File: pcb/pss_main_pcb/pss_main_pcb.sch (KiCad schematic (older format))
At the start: 0 parts

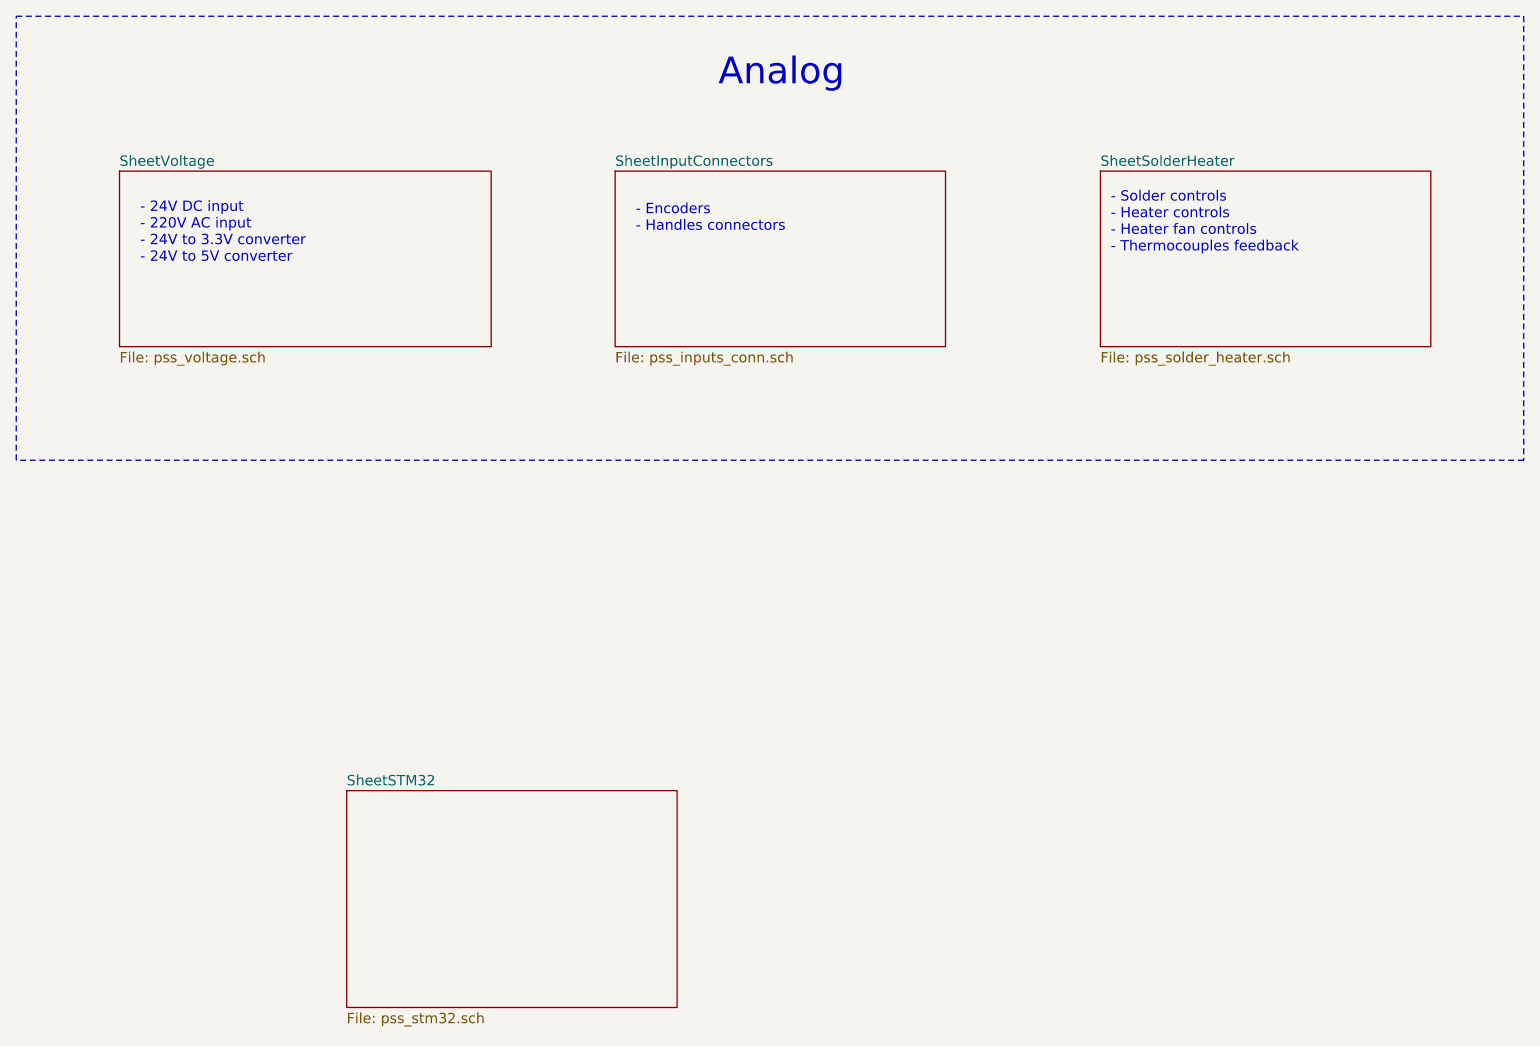
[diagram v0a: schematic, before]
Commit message: Add stm32 schematics
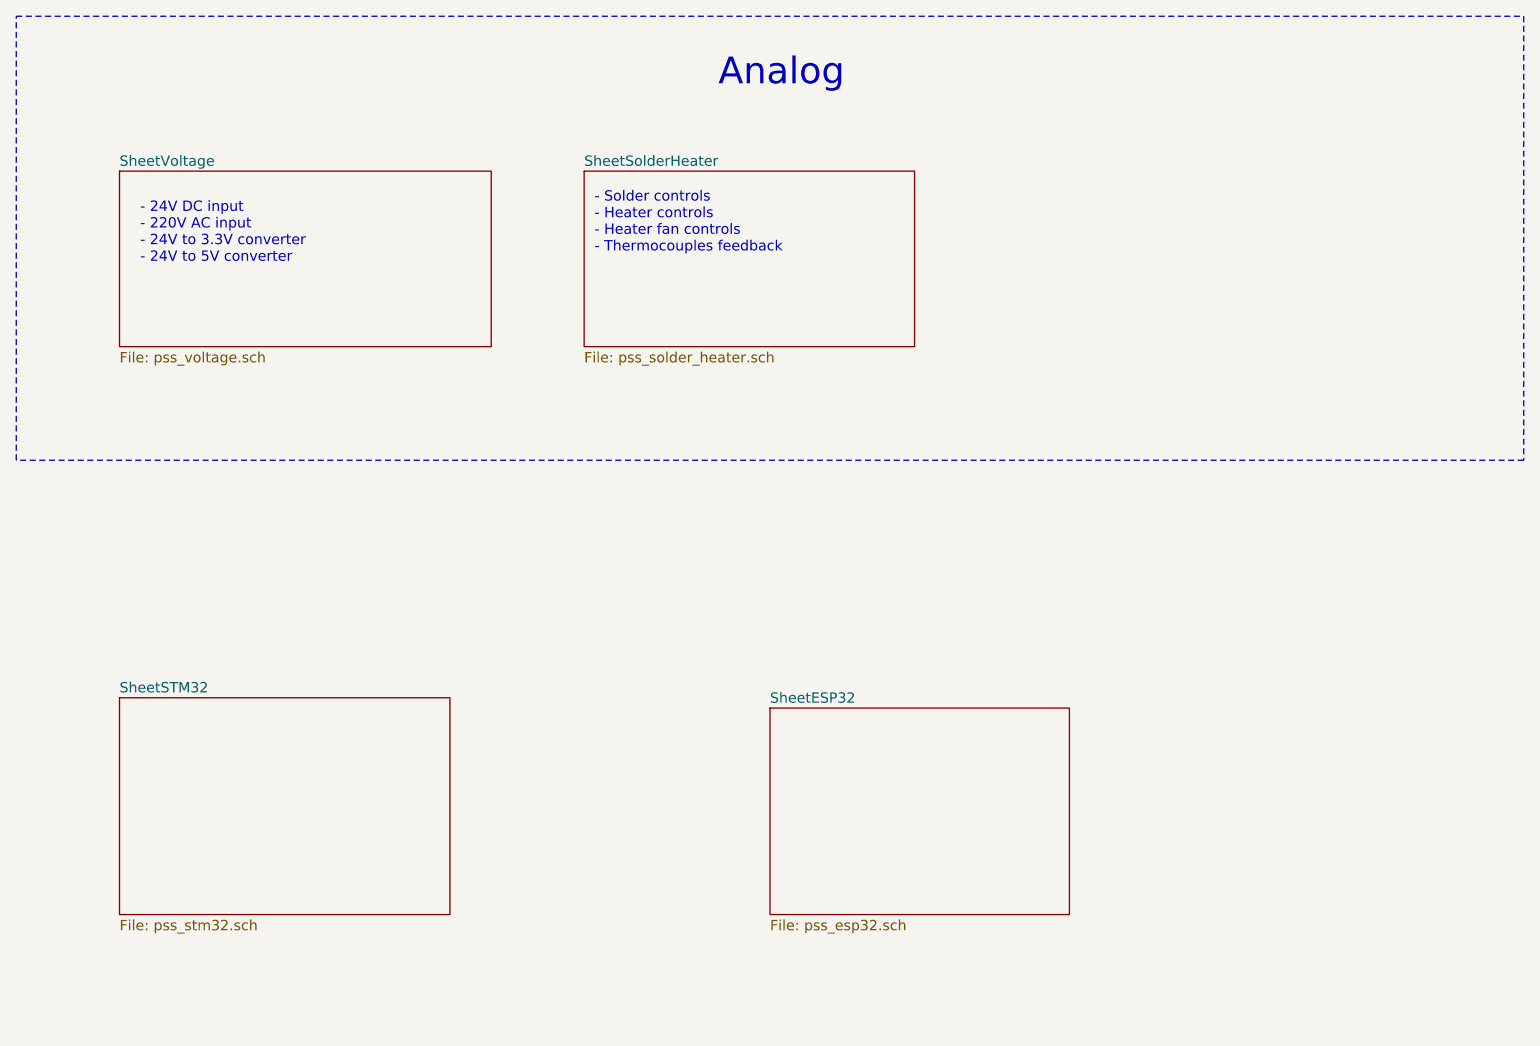
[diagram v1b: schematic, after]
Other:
- note removed: "- Encoders\n- Handles connectors"
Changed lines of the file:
@@
 EESchema Schematic File Version 4
-LIBS:pss_main_pcb-cache
-EELAYER 26 0
+EELAYER 30 0
 EELAYER END
 $Descr A4 11693 8268
@@
 $EndSheet
 $Sheet
-S 5450 1850 1600 850
-U 5EE027BC
-F0 "SheetInputConnectors" 50
-F1 "pss_inputs_conn.sch" 50
-$EndSheet
-$Sheet
-S 7800 1850 1600 850
+S 5300 1850 1600 850
 U 5EE1CBE0
 F0 "SheetSolderHeater" 50
@@
 Text Notes 3150 2300 0    50   ~ 0
 - 24V DC input\n- 220V AC input \n- 24V to 3.3V converter\n- 24V to 5V converter
-Text Notes 5550 2150 0    50   ~ 0
-- Encoders\n- Handles connectors
-Text Notes 7850 2250 0    50   ~ 0
+Text Notes 5350 2250 0    50   ~ 0
 - Solder controls\n- Heater controls\n- Heater fan controls\n- Thermocouples feedback\n
 Wire Notes Line
@@
 Analog
 $Sheet
-S 4150 4850 1600 1050
+S 3050 4400 1600 1050
 U 5EE5A305
 F0 "SheetSTM32" 50
 F1 "pss_stm32.sch" 50
 $EndSheet
+$Sheet
+S 6200 4450 1450 1000
+U 5ED3D5DF
+F0 "SheetESP32" 50
+F1 "pss_esp32.sch" 50
+$EndSheet
 $EndSCHEMATC

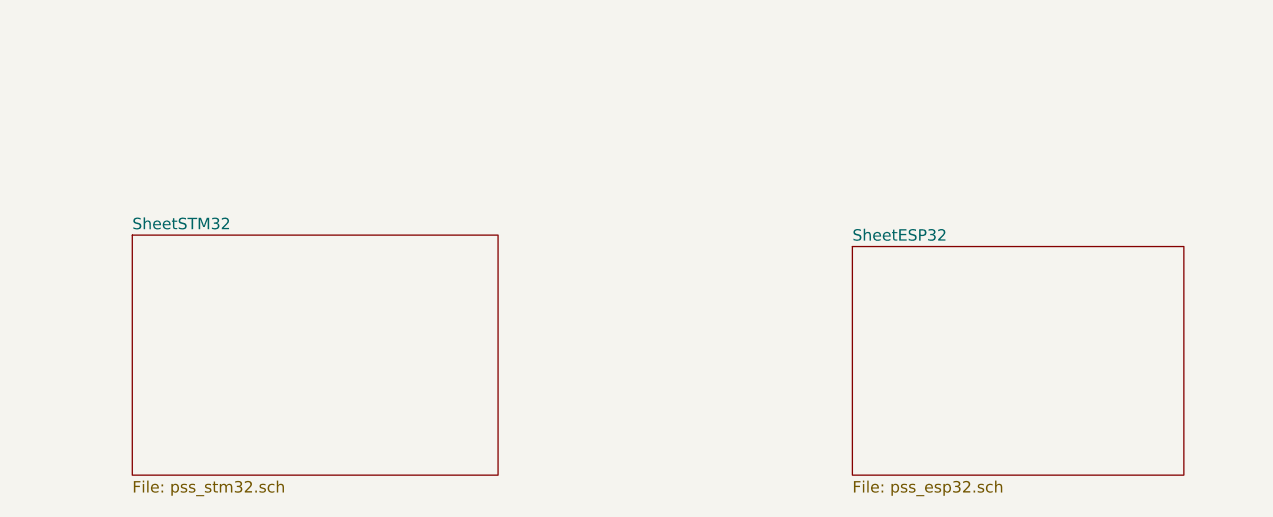
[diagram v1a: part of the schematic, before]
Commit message: Add ESP32 to display and STM32 connections
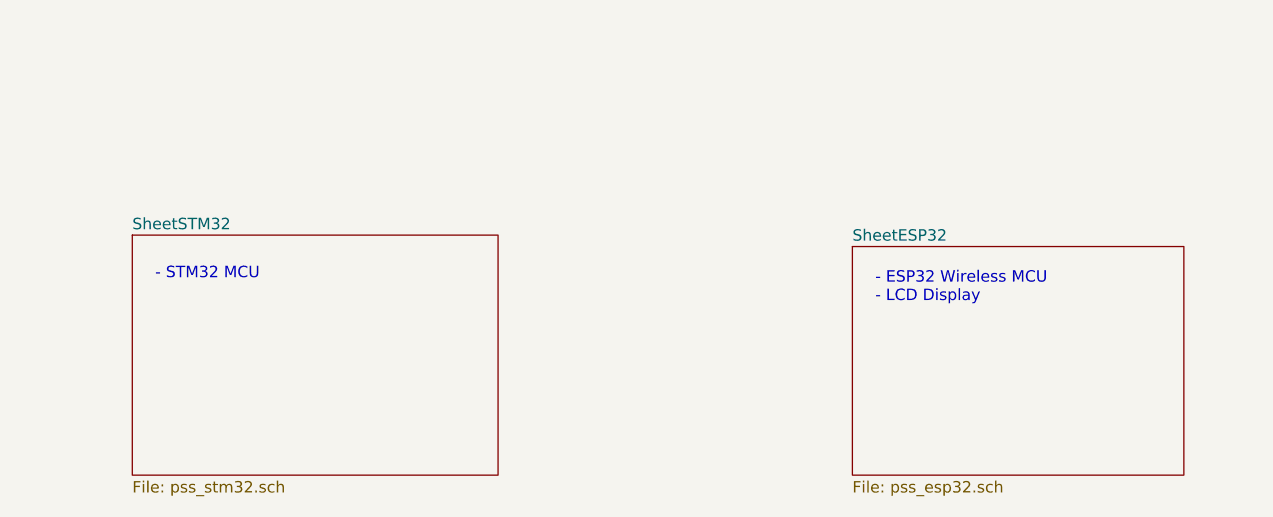
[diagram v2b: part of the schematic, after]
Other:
- note added: "- ESP32 Wireless MCU\n- LCD Display\n"
- note added: "- STM32 MCU\n"
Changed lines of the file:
@@
 F1 "pss_esp32.sch" 50
 $EndSheet
+Text Notes 3150 4600 0    50   ~ 0
+- STM32 MCU\n
+Text Notes 6300 4700 0    50   ~ 0
+- ESP32 Wireless MCU\n- LCD Display\n
 $EndSCHEMATC

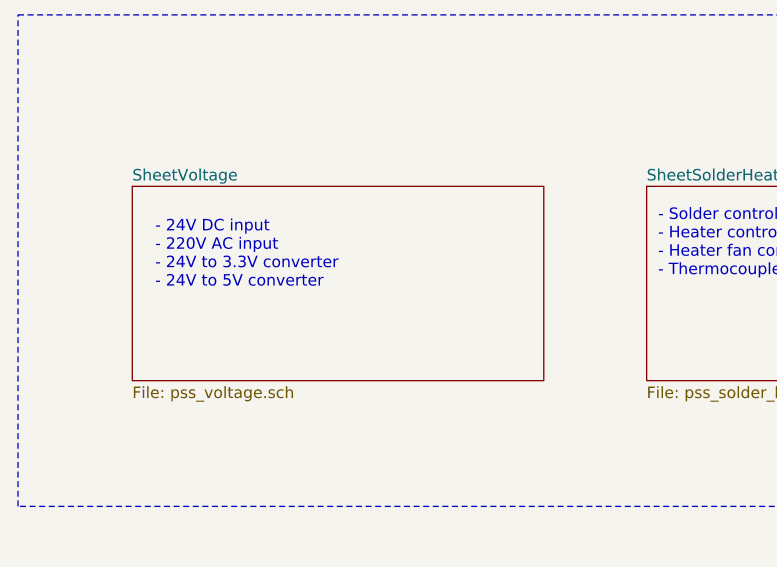
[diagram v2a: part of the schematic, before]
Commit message: Add new routes
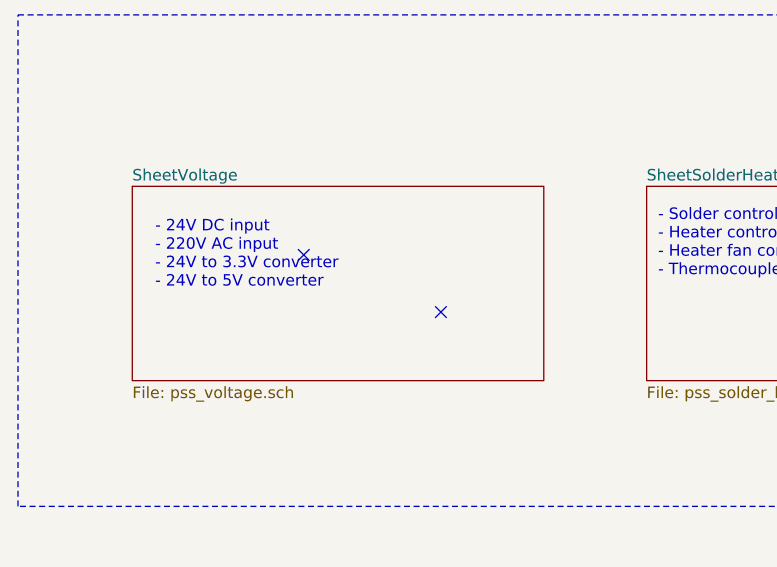
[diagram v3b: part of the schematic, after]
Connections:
- no-connect marks 0 -> 2
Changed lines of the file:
@@
 Text Notes 6300 4700 0    50   ~ 0
 - ESP32 Wireless MCU\n- LCD Display\n
+NoConn ~ 3800 2150
+NoConn ~ 4400 2400
 $EndSCHEMATC
